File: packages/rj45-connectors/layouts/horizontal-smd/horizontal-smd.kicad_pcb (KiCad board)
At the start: 2 copper layers, 3 parts

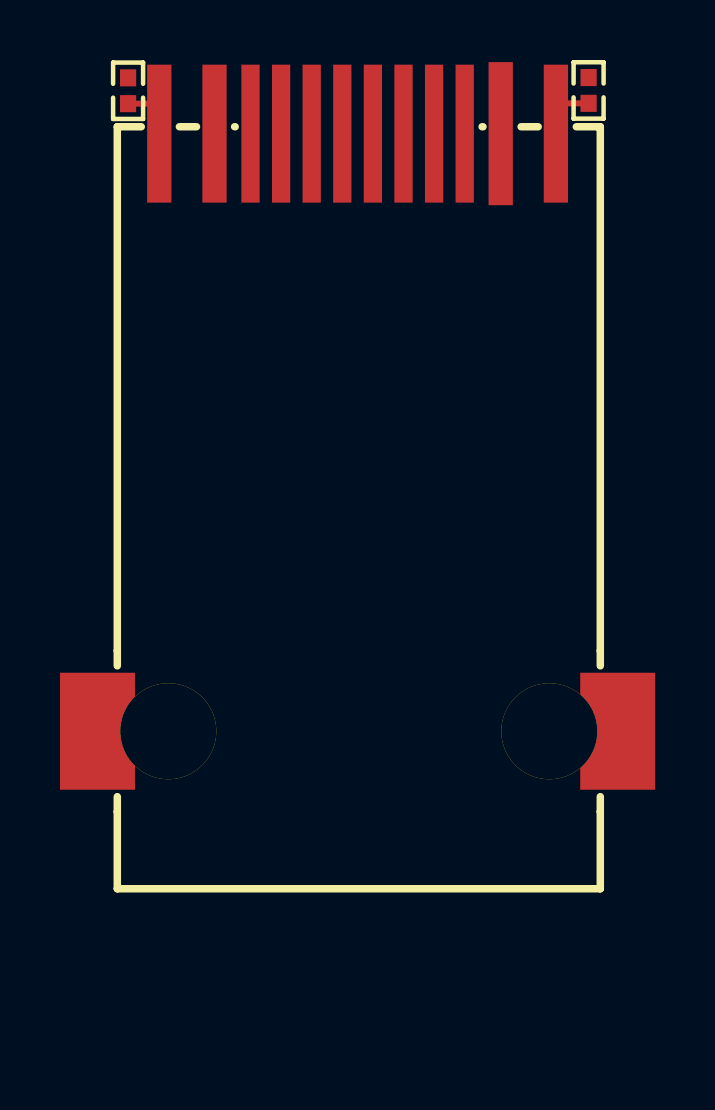
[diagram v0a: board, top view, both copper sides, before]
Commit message: rj45-connectors: fix shorted leds on 8port connector (#206)
* fix led short on 8port build target

* fix inconsistency
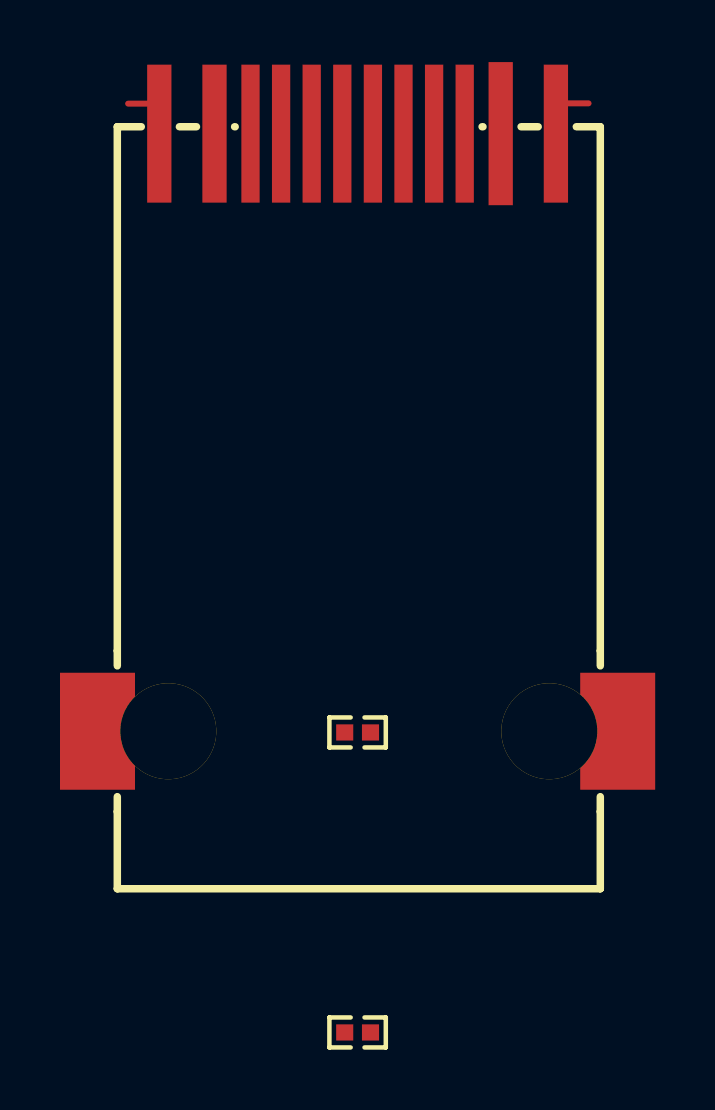
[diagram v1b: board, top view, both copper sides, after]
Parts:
- moved R1 32.3 mm to (0.00, 0.00), turned to 0 degrees
- moved R2 22.7 mm to (0.00, -10.0), turned to 0 degrees
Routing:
- net (no net): track 0.00 -> 4.14 mm
- net R_LEDYpos: track 2.15 -> 0.00 mm
- net L_LED_Gpos: track 1.99 -> 0.00 mm

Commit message: rj45-connectors: package update to v0.2.0, ato:^0.14.0
Build targets:
  8port = rc0
  default = rc0
  horizontal = rc0
  horizontal-smd = rc0
  recessed = rc0
  usage = rc0
  vertical = rc0
Package Verify: rc0
Version: 0.1.4 -> 0.2.0
Requires ato: ^0.14.0
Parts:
- R1, R2: value 470Ω ±1% 62.5mW -> 470.0Ω
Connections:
- net ETH_P0_N renamed ETH_N0_N
- net ETH_P1_N renamed ETH_N1_N
- net GND renamed lv
- RJ1 pad 7: footprint-net-1 -> (no net)
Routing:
- net 0: track 0.00 -> 4.14 mm
- net (no net): track 4.14 -> 0.00 mm

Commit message: manual fix package
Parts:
- R1, R2: value 470.0Ω -> 470Ω
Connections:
- RJ1 pad : footprint-net-0 -> (no net)
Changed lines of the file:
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@@
 			(drill 3.2)
 			(layers "*.Cu" "*.Mask")
-			(remove_unused_layers no)
-			(net 9 "footprint-net-0")
 		)
 		(pad "" thru_hole circle
@@
 			)
 		)
-		(property "Value" "470.0Ω"
+		(property "Value" "470Ω"
 			(at 0 4)
 			(layer "F.Fab")
@@
 			)
 		)
-		(property "resistance" "470.0±1.0%Ω"
-			(at 0 0 0)
-			(layer "User.9")
-			(hide yes)
-		)
-		(property "max_power" "0.0625W"
-			(at 0 0 0)
-			(layer "User.9")
-			(hide yes)
-		)
-		(property "max_voltage" "50.0V"
+		(property "resistance" "470±1.0%Ω"
+			(at 0 0 0)
+			(layer "User.9")
+			(hide yes)
+		)
+		(property "max_power" "0.062W"
+			(at 0 0 0)
+			(layer "User.9")
+			(hide yes)
+		)
+		(property "max_voltage" "50V"
 			(at 0 0 0)
 			(layer "User.9")
@@
 			)
 		)
-		(property "Value" "470.0Ω"
+		(property "Value" "470Ω"
 			(at 0 4)
 			(layer "F.Fab")
@@
 			)
 		)
-		(property "resistance" "470.0±1.0%Ω"
-			(at 0 0 0)
-			(layer "User.9")
-			(hide yes)
-		)
-		(property "max_power" "0.0625W"
-			(at 0 0 0)
-			(layer "User.9")
-			(hide yes)
-		)
-		(property "max_voltage" "50.0V"
-			(at 0 0 0)
-			(layer "User.9")
+		(property "resistance" "470±1.0%Ω"
+			(at 0 0 0)
+			(layer "User.9")
+			(hide yes)
+		)
+		(property "max_power" "0.062W"
+			(at 0 0 0)
+			(layer "User.9")
+			(hide yes)
+		)
+		(property "max_voltage" "50V"
+			(at 0 0 0)
+			(layer "User.9")
